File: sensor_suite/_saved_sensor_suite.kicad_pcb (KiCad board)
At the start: 4 copper layers, 71 parts, among them CN1 609-3634-ND, J1 Bar02, J10 Conn_01x01, J11 RJ45, J2 Conn_02x10_Counter_Clockwise, J3 Conn_01x02, J4 Conn_01x02, J5 LSM303, J6 Conn_02x20_Counter_Clockwise, J7 Conn_01x01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

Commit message: Finalized sensor board for ordering
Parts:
- removed C11, C12, C13, C14, C15, C16, C17, C18: 1 pF, Capacitor_SMD:C_0805_2012Metric
- removed C19, C21, C23, C25: 4.7 uF, Capacitor_SMD:C_0805_2012Metric
- removed C20, C22, C24, C26: 0.1 uF, Capacitor_SMD:C_0805_2012Metric
- removed J10, J9: Conn_01x01, ROV:RCA_Jack
- removed J11: RJ45, ROV:RJ45_Amphenol_54602-x08_Horizontal
- removed R10, R11, R12, R13, R14, R15, R16, R17, R18, R19, R20, R21, R22, R3, R4, R5, R6, R7, R8, R9: 50, Resistor_SMD:R_0805_2012Metric
- removed U4, U5, U6, U7: EL5173, ROV:EL5173ISZ
- J7: value Conn_01x01 -> Conn_01x03_Female; footprint ROV:RCA_Jack -> Connector_JST:JST_EH_B03B-EH-A_1x03_P2.50mm_Vertical
- J8: value Conn_01x01 -> Conn_01x10; footprint ROV:RCA_Jack -> Connector_PinHeader_2.54mm:PinHeader_1x10_P2.54mm_Vertical
- moved J7 77.6 mm to (143.5, 73.6), turned to 0 degrees
- moved J8 76.1 mm to (157.3, 79.1), turned to 0 degrees
- moved C9 19.0 mm to (179.2, 105.3), turned to 90 degrees
- moved C10 15.2 mm to (175.2, 105.3)
- moved C5 13.3 mm to (162.5, 100.5), turned to 0 degrees
- moved C6 12.1 mm to (166.2, 109.2), turned to 0 degrees
- moved J3 11.4 mm to (175.3, 73.6)
- moved J4 11.3 mm to (166.2, 73.6)
- moved C7 8.08 mm to (162.0, 108.8), turned to 270 degrees
- moved C4 7.97 mm to (172.7, 99.0), turned to 180 degrees
- moved C8 6.01 mm to (162.0, 104.7), turned to 270 degrees
- moved J1 3.41 mm to (152.3, 100.4)
- moved U3 0.16 mm to (182.6, 105.3)
- turned C2 to 180 degrees
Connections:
- CN1 pad 1: +12P -> Net-(CN1-Pad1)
- CN1 pad 2: +12P -> Net-(CN1-Pad2)
- CN1 pad 3: +12P -> Net-(CN1-Pad3)
- CN1 pad A3: PWM_4 -> PWM_3
- CN1 pad A5: PWM_8 -> PWM_13
- CN1 pad B3: PWM_5 -> PWM_2
- CN1 pad B5: PWM_9 -> PWM_15
- CN1 pad B6: PWM_13 -> PWM_14
- CN1 pad C3: PWM_6 -> PWM_8
- CN1 pad C4: PWM_2 -> PWM_9
- CN1 pad C5: PWM_10 -> PWM_11
- CN1 pad C6: PWM_14 -> PWM_10
- CN1 pad D3: PWM_7 -> PWM_4
- CN1 pad D4: PWM_3 -> PWM_5
- CN1 pad D5: PWM_11 -> PWM_6
- CN1 pad D6: PWM_15 -> PWM_7
- J2 pad 13: PWM_12 -> PWM_12_
- J2 pad 14: PWM_13 -> PWM_13_
- J2 pad 15: PWM_14 -> PWM_14_
- J2 pad 16: PWM_15 -> PWM_15_
- J6 pad 2: Net-(J6-Pad2) -> +5VP
- J6 pad 6: Net-(J6-Pad6) -> GNDPWR
- J7 pad 1: Net-(J7-Pad1) -> +5VP
- J7 pad 2: (no net) -> GNDPWR
- J8 pad 1: Net-(J8-Pad1) -> +5VP
- J8 pad 2: (no net) -> GNDPWR
- JP1 pad 1: PWM_13 -> PWM_13_
- JP2 pad 1: PWM_12 -> PWM_12_
- JP3 pad 1: PWM_14 -> PWM_14_
- JP4 pad 1: PWM_15 -> PWM_15_
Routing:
- net GNDPWR: track 177.0 -> 16.3 mm, vias 10 -> 2
- net Net-(C12-Pad1): track 84.9 -> 0.00 mm
- net Net-(C11-Pad1): track 78.7 -> 0.00 mm
- net Net-(C14-Pad1): track 71.2 -> 0.00 mm
- net Net-(C13-Pad1): track 63.6 -> 0.00 mm
- net Net-(C16-Pad1): track 49.7 -> 0.00 mm
- net Net-(C15-Pad1): track 44.3 -> 0.00 mm
- net Net-(C18-Pad1): track 35.9 -> 0.00 mm
- net PWM_14: track 63.2 -> 27.6 mm
- net PWM_14_: track 0.00 -> 32.5 mm
- net PWM_12: track 73.7 -> 42.8 mm
- net PWM_13_: track 0.00 -> 30.1 mm
- net PWM_13: track 68.1 -> 38.1 mm
- net Net-(J7-Pad3): track 0.00 -> 29.6 mm
- net PWM_12_: track 0.00 -> 29.4 mm
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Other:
- board outline added: 80.2 x 82.3 mm
- board text added: "Bar02"
- board text added: "LM303"
- board text removed: "anode"
- board text removed: "|"

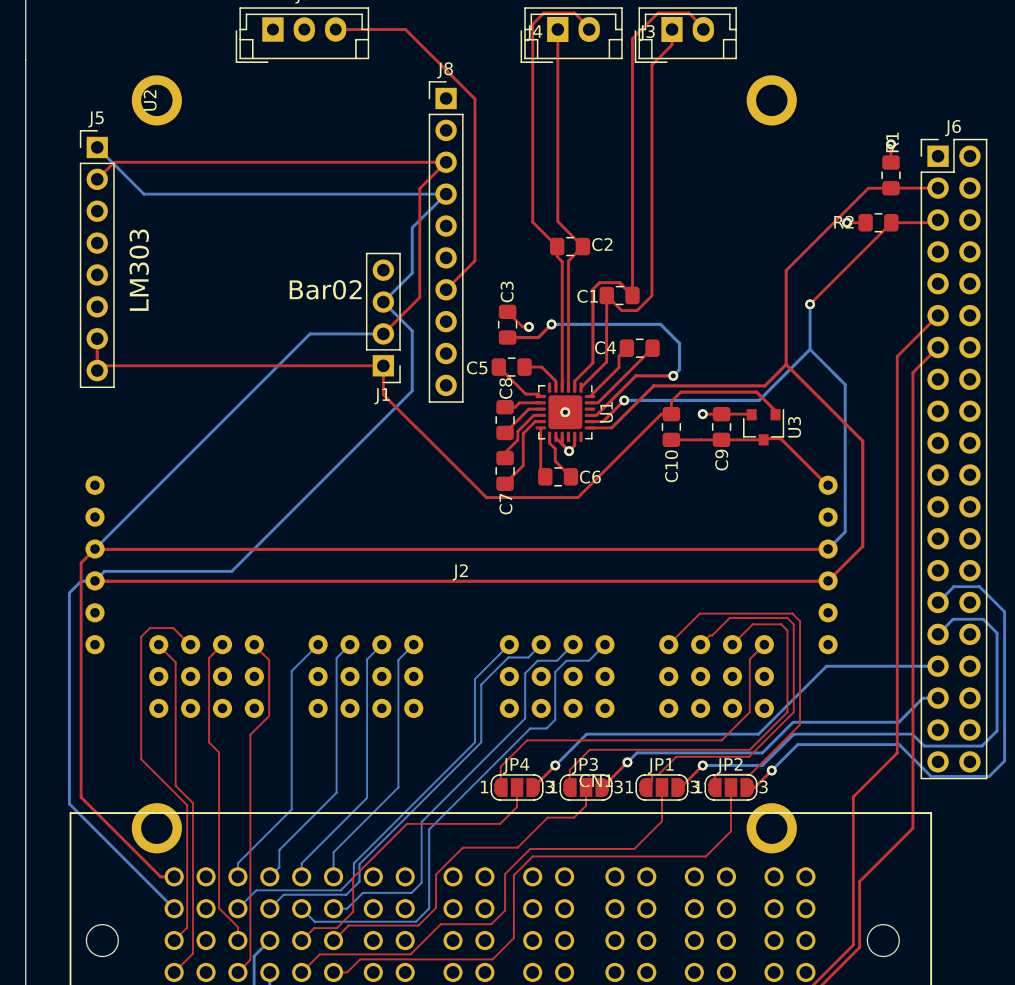
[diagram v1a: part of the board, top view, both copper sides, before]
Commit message: Swapped out Gyro
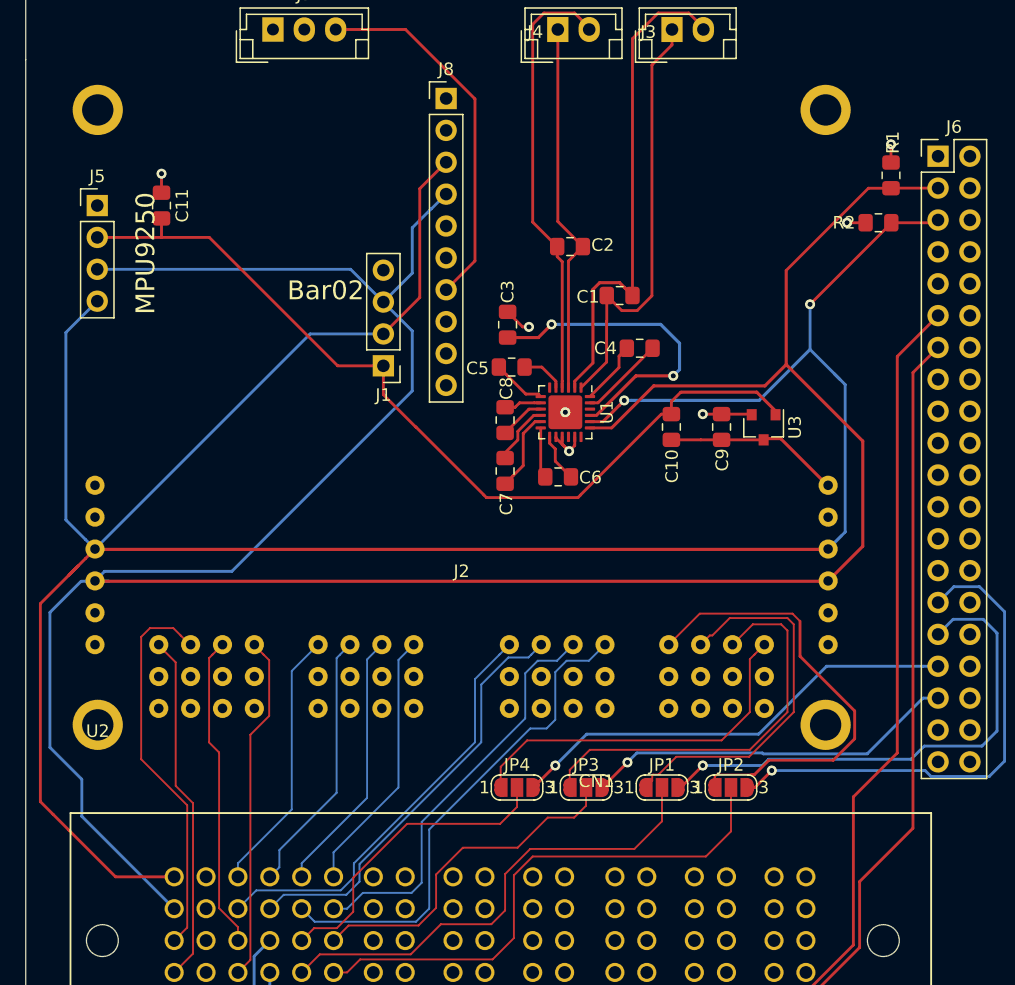
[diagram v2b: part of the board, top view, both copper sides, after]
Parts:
- added C11: C_Small, Capacitor_SMD:C_0805_2012Metric_Pad1.15x1.40mm_HandSolder, F.Cu at (134.6, 87.6)
- J5: value LSM303 -> Conn_01x04_Female; footprint Connector_PinHeader_2.54mm:PinHeader_1x08_P2.54mm_Vertical -> Connector_PinHeader_2.54mm:PinHeader_1x04_P2.54mm_Vertical
- U2: footprint ROV:Pi3+ -> rov:Pi3+
- moved U2 50.0 mm to (129.5, 129.0), turned to 0 degrees
- moved J5 4.63 mm to (129.5, 87.6)
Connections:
- J5 pad 1: SDA_iso -> GNDPWR
- J5 pad 2: SCL_iso -> +3V3
- J5 pad 3: Net-(J5-Pad3) -> SDA_iso
- J5 pad 4: Net-(J5-Pad4) -> SCL_iso
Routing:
- net PWM_12_: track 29.4 -> 36.4 mm
- net SDA_iso: track 231.2 -> 227.0 mm
- net +3V3: track 67.8 -> 70.4 mm
- net DigitalOutput3: track 42.0 -> 40.3 mm
- net GNDPWR: track 16.3 -> 17.8 mm, vias 2 -> 3
- net DigitalOutput4: track 41.5 -> 40.7 mm
- net SCL_iso: track 217.7 -> 217.0 mm
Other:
- board text added: "MPU9250"
- board text removed: "LM303"

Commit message: sensor board
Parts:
- added F1: Fuse, Fuse:Fuse_1812_4532Metric_Pad1.30x3.40mm_HandSolder, F.Cu at (196.8, 79.5)
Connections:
- J6 pad 2: +5VP -> Net-(F1-Pad2)
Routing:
- net +5VP: track 11.2 -> 9.79 mm
- added copper zone on F.Cu, net +5VP
- added copper zone on F.Cu, net Net-(F1-Pad2)
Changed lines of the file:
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@@
     (tracks 437)
     (zones 0)
-    (modules 29)
-    (nets 89)
+    (modules 30)
+    (nets 90)
   )
   (page A4)
@@
       (drillshape 0)
       (scaleselection 1)
-      (outputdirectory "Gerbers -21-19/"))
+      (outputdirectory "../../../../../../Volumes/Files-Data/Clubs/IEEE/EE-2019/sensor_suite/Gerbers 3-6-19/"))
   )
   (net 0 "")
@@
   (net 87 "Net-(CN1-Pad2)")
   (net 88 "Net-(CN1-Pad1)")
+  (net 89 "Net-(F1-Pad2)")
   (net_class Default "This is the default net class."
     (clearance 0.2)
@@
     (add_net "Net-(CN1-Pad2)")
     (add_net "Net-(CN1-Pad3)")
+    (add_net "Net-(F1-Pad2)")
     (add_net "Net-(J6-Pad1)")
     (add_net "Net-(J6-Pad10)")
@@
     (add_net PWM_9)
   )
+  (module Fuse:Fuse_1812_4532Metric_Pad1.30x3.40mm_HandSolder (layer F.Cu)
+    (at 196.85 79.502)
+    (descr "Fuse SMD 1812 (4532 Metric), square (rectangular) end terminal, IPC_7351 nominal with elongated pad for handsoldering. (Body size source: https://www.nikhef.nl/pub/departments/mt/projects/detectorR_D/dtddice/ERJ2G.pdf), generated with kicad-footprint-generator")
+    (tags "resistor handsolder")
+    (attr smd)
+    (fp_text reference F1 (at 0 -2.65) (layer F.SilkS)
+      (effects (font (size 1 1) (thickness 0.15)))
+    )
+    (fp_text value Fuse (at 0 2.65) (layer F.Fab)
+      (effects (font (size 1 1) (thickness 0.15)))
+    )
+    (fp_line (start -2.25 1.6) (end -2.25 -1.6) (layer F.Fab) (width 0.1))
+    (fp_line (start -2.25 -1.6) (end 2.25 -1.6) (layer F.Fab) (width 0.1))
+    (fp_line (start 2.25 -1.6) (end 2.25 1.6) (layer F.Fab) (width 0.1))
+    (fp_line (start 2.25 1.6) (end -2.25 1.6) (layer F.Fab) (width 0.1))
+    (fp_line (start -1.386252 -1.71) (end 1.386252 -1.71) (layer F.SilkS) (width 0.12))
+    (fp_line (start -1.386252 1.71) (end 1.386252 1.71) (layer F.SilkS) (width 0.12))
+    (fp_line (start -3.12 1.95) (end -3.12 -1.95) (layer F.CrtYd) (width 0.05))
+    (fp_line (start -3.12 -1.95) (end 3.12 -1.95) (layer F.CrtYd) (width 0.05))
+    (fp_line (start 3.12 -1.95) (end 3.12 1.95) (layer F.CrtYd) (width 0.05))
+    (fp_line (start 3.12 1.95) (end -3.12 1.95) (layer F.CrtYd) (width 0.05))
+    (fp_text user %R (at 0 0) (layer F.Fab)
+      (effects (font (size 1 1) (thickness 0.15)))
+    )
+    (pad 1 smd roundrect (at -2.225 0) (size 1.3 3.4) (layers F.Cu F.Paste F.Mask) (roundrect_rratio 0.192308)
+      (net 2 +5VP))
+    (pad 2 smd roundrect (at 2.225 0) (size 1.3 3.4) (layers F.Cu F.Paste F.Mask) (roundrect_rratio 0.192308)
+      (net 89 "Net-(F1-Pad2)"))
+    (model ${KISYS3DMOD}/Fuse.3dshapes/Fuse_1812_4532Metric.wrl
+      (at (xyz 0 0 0))
+      (scale (xyz 1 1 1))
+      (rotate (xyz 0 0 0))
+    )
+  )
   (module rov:Pi3+ (layer F.Cu)
     (at 129.54 129.01)
@@
       (net 24 "Net-(J6-Pad1)"))
     (pad 2 thru_hole oval (at 2.54 0) (size 1.7 1.7) (drill 1) (layers *.Cu *.Mask)
-      (net 2 +5VP))
+      (net 89 "Net-(F1-Pad2)"))
     (pad 3 thru_hole oval (at 0 2.54) (size 1.7 1.7) (drill 1) (layers *.Cu *.Mask)
       (net 51 SDA_iso))
@@
   (via (at 134.62 85.09) (size 0.8) (drill 0.4) (layers F.Cu B.Cu) (net 1))
   (segment (start 134.62 86.605) (end 134.62 85.09) (width 0.2286) (layer F.Cu) (net 1))
-  (via (at 192.75 82.75) (size 0.8) (drill 0.4) (layers F.Cu B.Cu) (net 2))
+  (via (at 192.532 80.01) (size 0.8) (drill 0.4) (layers F.Cu B.Cu) (net 2))
   (via (at 189.25 89) (size 0.8) (drill 0.4) (layers F.Cu B.Cu) (net 2))
   (via (at 167.1 107.2) (size 0.8) (drill 0.4) (layers F.Cu B.Cu) (net 2))
-  (segment (start 192.75 84.2) (end 192.75 82.75) (width 0.2286) (layer F.Cu) (net 2))
   (segment (start 189.25 89) (end 190.725 89) (width 0.2286) (layer F.Cu) (net 2))
   (segment (start 167.55 106.75) (end 167.1 107.2) (width 0.2286) (layer F.Cu) (net 2))
@@
   (segment (start 159.6 92.04) (end 159.6 79.134258) (width 0.2286) (layer F.Cu) (net 82))
   (segment (start 154.065742 73.6) (end 148.5 73.6) (width 0.2286) (layer F.Cu) (net 82))
+  (segment (start 199.04 79.537) (end 199.075 79.502) (width 0.2286) (layer F.Cu) (net 89))
   (zone (net 2) (net_name +5VP) (layer In1.Cu) (hatch edge 0.508)
     (connect_pads yes (clearance 0.508))
@@
       )
     )
+  )
+  (zone (net 2) (net_name +5VP) (layer F.Cu) (hatch edge 0.508)
+    (connect_pads yes (clearance 0.508))
+    (min_thickness 0.254)
+    (fill yes (arc_segments 16) (thermal_gap 0.508) (thermal_bridge_width 0.508))
+    (polygon
+      (pts
+        (xy 195.58 77.216) (xy 195.58 81.788) (xy 193.802 81.788) (xy 193.802 85.09) (xy 191.77 85.09)
+        (xy 191.77 77.216)
+      )
+    )
+  )
+  (zone (net 89) (net_name "Net-(F1-Pad2)") (layer F.Cu) (hatch edge 0.508)
+    (connect_pads yes (clearance 0.508))
+    (min_thickness 0.254)
+    (fill yes (arc_segments 16) (thermal_gap 0.508) (thermal_bridge_width 0.508))
+    (polygon
+      (pts
+        (xy 198.12 77.724) (xy 198.12 84.328) (xy 199.898 84.328) (xy 199.898 77.724)
+      )
+    )
